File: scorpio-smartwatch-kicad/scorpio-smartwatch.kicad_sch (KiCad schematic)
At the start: 5 parts, among them IC1 LSM6DSV80XTR, U1 nRF52840, U2 MIA-M10Q, U3 LIS2MDL

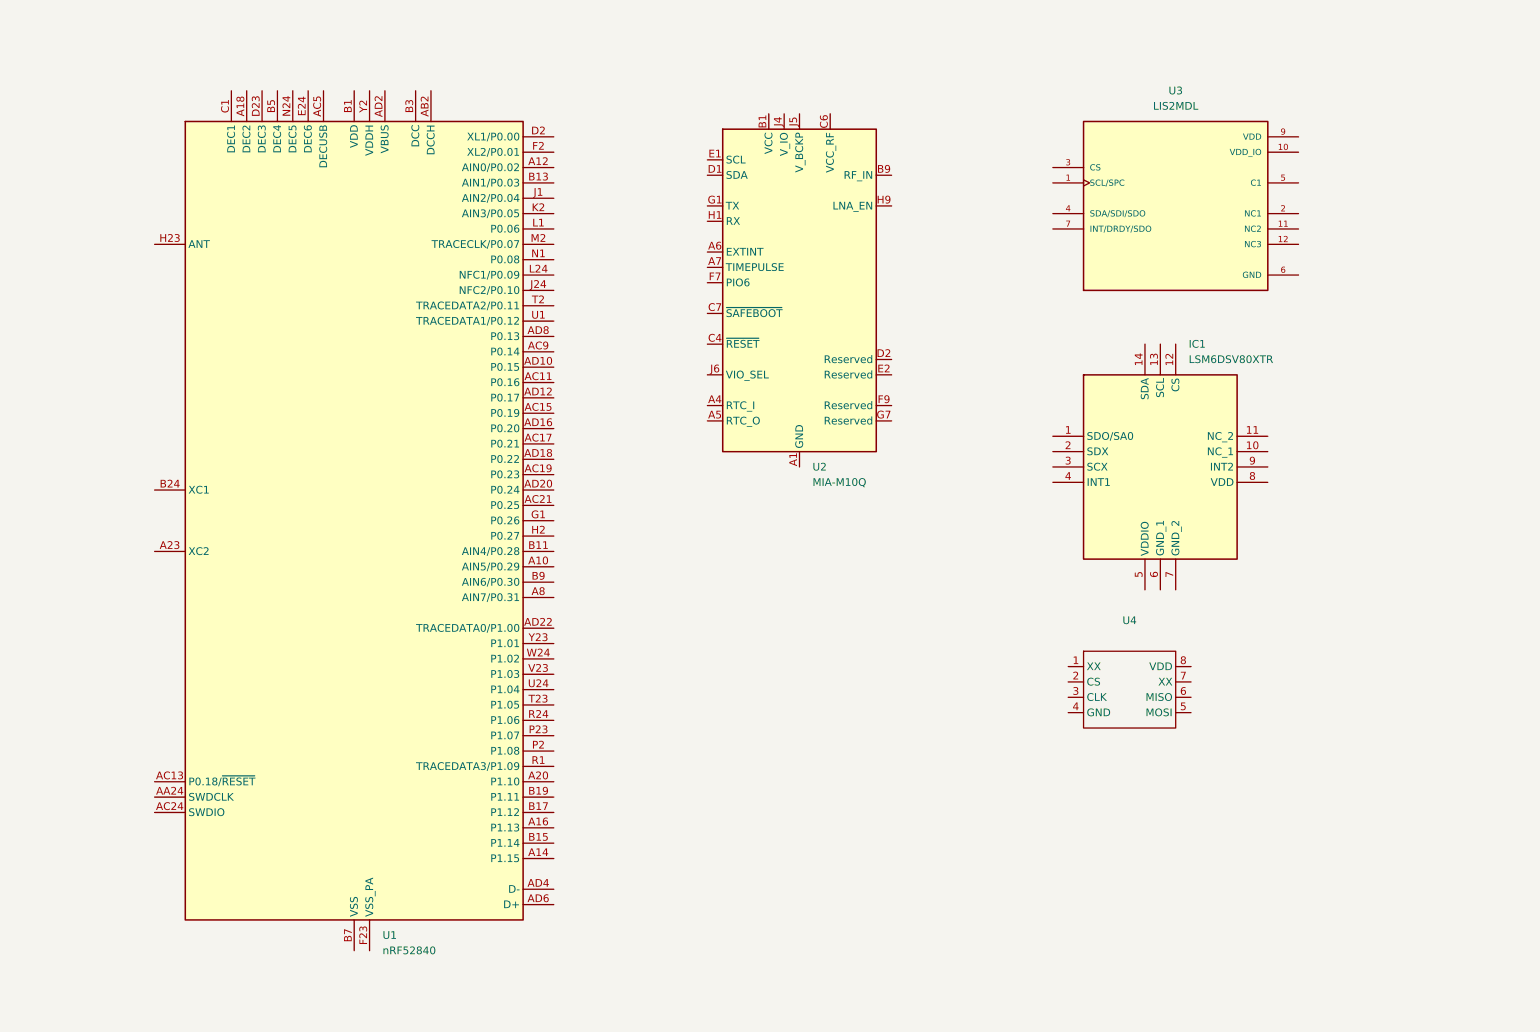
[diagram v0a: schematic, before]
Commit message: Adding dimensions on the pcb and adding tables for current and battery sizes. need to change NRF footprint still. Need to add: Buttons, Screen Connector / Driver, HR connector (I2C), Power Management, Battery Connector, Mounting Holes, Passives.
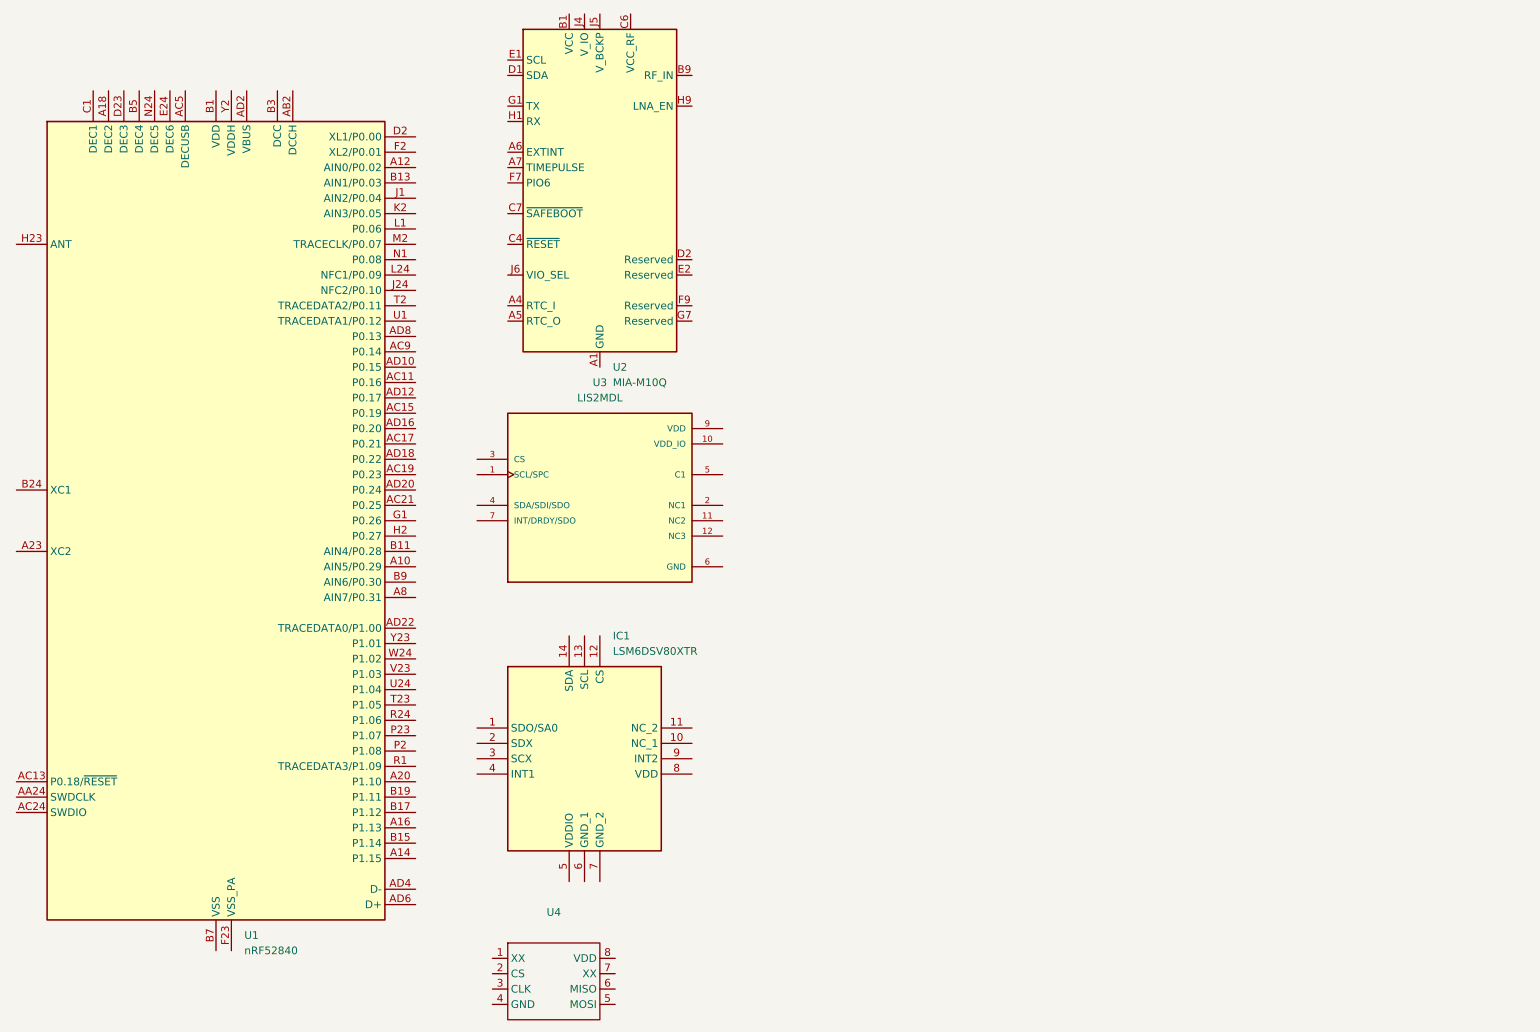
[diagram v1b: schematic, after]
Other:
- moved on the sheet: IC1, U1, U2, U3, U4

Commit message: minor changes
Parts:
- removed U1: nRF52840, Package_DFN_QFN:Nordic_AQFN-73-1EP_7x7mm_P0.5mm, symbol MCU_Nordic:nRF52840
- added IC2: NRF52840-QFAA-F-R, RF_Module:QFN40P600X600X95-49N-D, symbol MCU_Nordic:NRF52840-QFAA-F-R
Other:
- note added: "NEEDS: - Chip antennas - Buttons - Display Connector - HR Sensor Connector (I2C) - Programming Header (JTAG / SWD) - Power LED - Status LED - Power Connection - Battery Charger - Passives"
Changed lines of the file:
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@@
 	(generator_version "9.0")
 	(paper "A4")
+	(text "NEEDS:\n- Chip antennas\n- Buttons\n- Display Connector\n- HR Sensor Connector (I2C)\n- Programming Header (JTAG / SWD)\n- Power LED\n- Status LED\n- Power Connection\n- Battery Charger\n- Passives"
+		(exclude_from_sim no)
+		(at 166.624 101.092 0)
+		(effects
+			(font
+				(size 3 3)
+				(thickness 0.6)
+				(bold yes)
+			)
+			(justify left)
+		)
+	)
 	(table
 		(column_count 3)
@@
 					)
 					(justify left top)
-				)
-			)
-		)
-	)
-	(symbol
-		(lib_id "MCU_Nordic:nRF52840")
-		(at 54.61 104.14 0)
-		(unit 1)
-		(exclude_from_sim no)
-		(in_bom yes)
-		(on_board yes)
-		(dnp no)
-		(fields_autoplaced yes)
-		(property "Reference" "U1"
-			(at 59.2933 172.72 0)
-			(effects
-				(font
-					(size 1.27 1.27)
-				)
-				(justify left)
-			)
-		)
-		(property "Value" "nRF52840"
-			(at 59.2933 175.26 0)
-			(effects
-				(font
-					(size 1.27 1.27)
-				)
-				(justify left)
-			)
-		)
-		(property "Footprint" "Package_DFN_QFN:Nordic_AQFN-73-1EP_7x7mm_P0.5mm"
-			(at 54.61 177.8 0)
-			(effects
-				(font
-					(size 1.27 1.27)
-				)
-				(hide yes)
-			)
-		)
-		(property "Datasheet" "http://infocenter.nordicsemi.com/topic/com.nordic.infocenter.nrf52/dita/nrf52/chips/nrf52840.html"
-			(at 38.1 55.88 0)
-			(effects
-				(font
-					(size 1.27 1.27)
-				)
-				(hide yes)
-			)
-		)
-		(property "Description" "Multiprotocol BLE/ANT/2.4 GHz/802.15.4 Cortex-M4F SoC, AQFN-73"
-			(at 54.61 104.14 0)
-			(effects
-				(font
-					(size 1.27 1.27)
-				)
-				(hide yes)
-			)
-		)
-		(pin "B7"
-		)
-		(pin "E24"
-		)
-		(pin "AD2"
-		)
-		(pin "B3"
-		)
-		(pin "AB2"
-		)
-		(pin "D2"
-		)
-		(pin "F2"
-		)
-		(pin "A12"
-		)
-		(pin "B13"
-		)
-		(pin "J1"
-		)
-		(pin "K2"
-		)
-		(pin "L1"
-		)
-		(pin "M2"
-		)
-		(pin "N1"
-		)
-		(pin "L24"
-		)
-		(pin "J24"
-		)
-		(pin "Y2"
-		)
-		(pin "F23"
-		)
-		(pin "B1"
-		)
-		(pin "AD23"
-		)
-		(pin "AC5"
-		)
-		(pin "AA24"
-		)
-		(pin "AC24"
-		)
-		(pin "T2"
-		)
-		(pin "U1"
-		)
-		(pin "AD8"
-		)
-		(pin "AC9"
-		)
-		(pin "AD10"
-		)
-		(pin "AC11"
-		)
-		(pin "AD12"
-		)
-		(pin "AC15"
-		)
-		(pin "AD16"
-		)
-		(pin "AC17"
-		)
-		(pin "AD18"
-		)
-		(pin "AC19"
-		)
-		(pin "AD20"
-		)
-		(pin "AC21"
-		)
-		(pin "G1"
-		)
-		(pin "H2"
-		)
-		(pin "B11"
-		)
-		(pin "A10"
-		)
-		(pin "B9"
-		)
-		(pin "A8"
-		)
-		(pin "AD22"
-		)
-		(pin "Y23"
-		)
-		(pin "W24"
-		)
-		(pin "V23"
-		)
-		(pin "U24"
-		)
-		(pin "T23"
-		)
-		(pin "R24"
-		)
-		(pin "P23"
-		)
-		(pin "P2"
-		)
-		(pin "R1"
-		)
-		(pin "A20"
-		)
-		(pin "B19"
-		)
-		(pin "B17"
-		)
-		(pin "A16"
-		)
-		(pin "B15"
-		)
-		(pin "A14"
-		)
-		(pin "AD4"
-		)
-		(pin "AD6"
-		)
-		(pin "AC13"
-		)
-		(pin "AD14"
-		)
-		(pin "C1"
-		)
-		(pin "B5"
-		)
-		(pin "A22"
-		)
-		(pin "A23"
-		)
-		(pin "B24"
-		)
-		(pin "H23"
-		)
-		(pin "W1"
-		)
-		(pin "N24"
-		)
-		(pin "A18"
-		)
-		(pin "EP"
-		)
-		(pin "D23"
-		)
-		(instances
-			(project ""
-				(path "/96827652-e1e2-460c-809b-37b17a1aacc0"
-					(reference "U1")
-					(unit 1)
 				)
 			)
@@
 					(unit 1)
 				)
+			)
+		)
+	)
+	(symbol
+		(lib_id "MCU_Nordic:NRF52840-QFAA-F-R")
+		(at 27.94 85.09 0)
+		(unit 1)
+		(exclude_from_sim no)
+		(in_bom yes)
+		(on_board yes)
+		(dnp no)
+		(fields_autoplaced yes)
+		(property "Reference" "IC2"
+			(at 86.36 78.6698 0)
+			(effects
+				(font
+					(size 1.27 1.27)
+				)
+			)
+		)
+		(property "Value" "NRF52840-QFAA-F-R"
+			(at 86.36 81.2098 0)
+			(effects
+				(font
+					(size 1.27 1.27)
+				)
+			)
+		)
+		(property "Footprint" "RF_Module:QFN40P600X600X95-49N-D"
+			(at 74.93 164.77 0)
+			(effects
+				(font
+					(size 1.27 1.27)
+				)
+				(justify left top)
+				(hide yes)
+			)
+		)
+		(property "Datasheet" "https://docs-be.nordicsemi.com/bundle/ps_nrf52840/attach/nRF52840_PS_v1.11.pdf?_LANG=enus"
+			(at 74.93 264.77 0)
+			(effects
+				(font
+					(size 1.27 1.27)
+				)
+				(justify left top)
+				(hide yes)
+			)
+		)
+		(property "Description" "RF System on a Chip - SoC Multiprotocol Bluetooth 5.3 SoC supporting Bluetooth Low Energy, Bluetooth mesh, NFC, Thread and Zigbee"
+			(at 27.94 85.09 0)
+			(effects
+				(font
+					(size 1.27 1.27)
+				)
+				(hide yes)
+			)
+		)
+		(property "Height" "0.95"
+			(at 74.93 464.77 0)
+			(effects
+				(font
+					(size 1.27 1.27)
+				)
+				(justify left top)
+				(hide yes)
+			)
+		)
+		(property "Mouser Part Number" "949-NRF52840QFAA-R"
+			(at 74.93 564.77 0)
+			(effects
+				(font
+					(size 1.27 1.27)
+				)
+				(justify left top)
+				(hide yes)
+			)
+		)
+		(property "Mouser Price/Stock" "https://www.mouser.co.uk/ProductDetail/Nordic-Semiconductor/NRF52840-QFAA-F-R?qs=A6eO%252BMLsxmSdeoxcrQ6IBg%3D%3D"
+			(at 74.93 664.77 0)
+			(effects
+				(font
+					(size 1.27 1.27)
+				)
+				(justify left top)
+				(hide yes)
+			)
+		)
+		(property "Manufacturer_Name" "Nordic Semiconductor"
+			(at 74.93 764.77 0)
+			(effects
+				(font
+					(size 1.27 1.27)
+				)
+				(justify left top)
+				(hide yes)
+			)
+		)
+		(property "Manufacturer_Part_Number" "NRF52840-QFAA-F-R"
+			(at 74.93 864.77 0)
+			(effects
+				(font
+					(size 1.27 1.27)
+				)
+				(justify left top)
+				(hide yes)
+			)
+		)
+		(pin "46"
+		)
+		(pin "28"
+		)
+		(pin "27"
+		)
+		(pin "26"
+		)
+		(pin "25"
+		)
+		(pin "34"
+		)
+		(pin "33"
+		)
+		(pin "32"
+		)
+		(pin "31"
+		)
+		(pin "30"
+		)
+		(pin "29"
+		)
+		(pin "37"
+		)
+		(pin "36"
+		)
+		(pin "35"
+		)
+		(pin "23"
+		)
+		(pin "38"
+		)
+		(pin "24"
+		)
+		(pin "10"
+		)
+		(pin "49"
+		)
+		(pin "17"
+		)
+		(pin "44"
+		)
+		(pin "9"
+		)
+		(pin "8"
+		)
+		(pin "7"
+		)
+		(pin "6"
+		)
+		(pin "20"
+		)
+		(pin "2"
+		)
+		(pin "3"
+		)
+		(pin "11"
+		)
+		(pin "14"
+		)
+		(pin "5"
+		)
+		(pin "4"
+		)
+		(pin "45"
+		)
+		(pin "48"
+		)
+		(pin "12"
+		)
+		(pin "15"
+		)
+		(pin "16"
+		)
+		(pin "1"
+		)
+		(pin "41"
+		)
+		(pin "21"
+		)
+		(pin "40"
+		)
+		(pin "19"
+		)
+		(pin "22"
+		)
+		(pin "43"
+		)
+		(pin "39"
+		)
+		(pin "42"
+		)
+		(pin "47"
+		)
+		(pin "18"
+		)
+		(pin "13"
+		)
+		(instances
+			(project ""
+				(path "/96827652-e1e2-460c-809b-37b17a1aacc0"
+					(reference "IC2")
+					(unit 1)
+				)

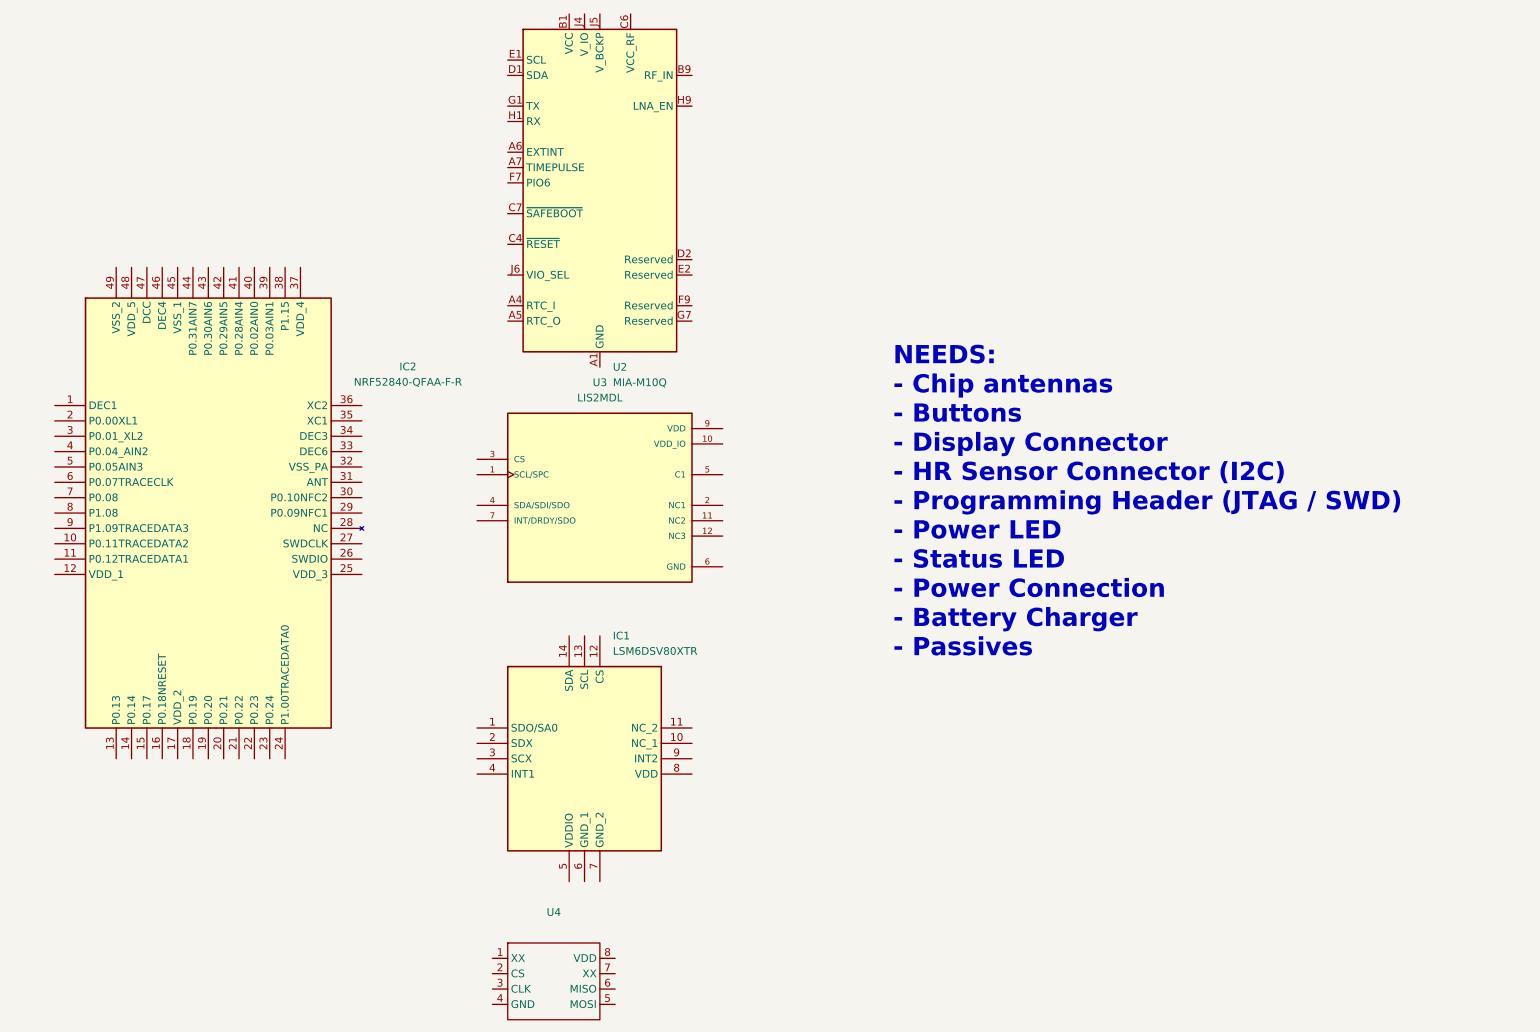
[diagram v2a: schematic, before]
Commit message: wip commit, added chip antenna, trying out different pcb sizes. not routing until we can figure out the rf nightmare with ground plane sizes.
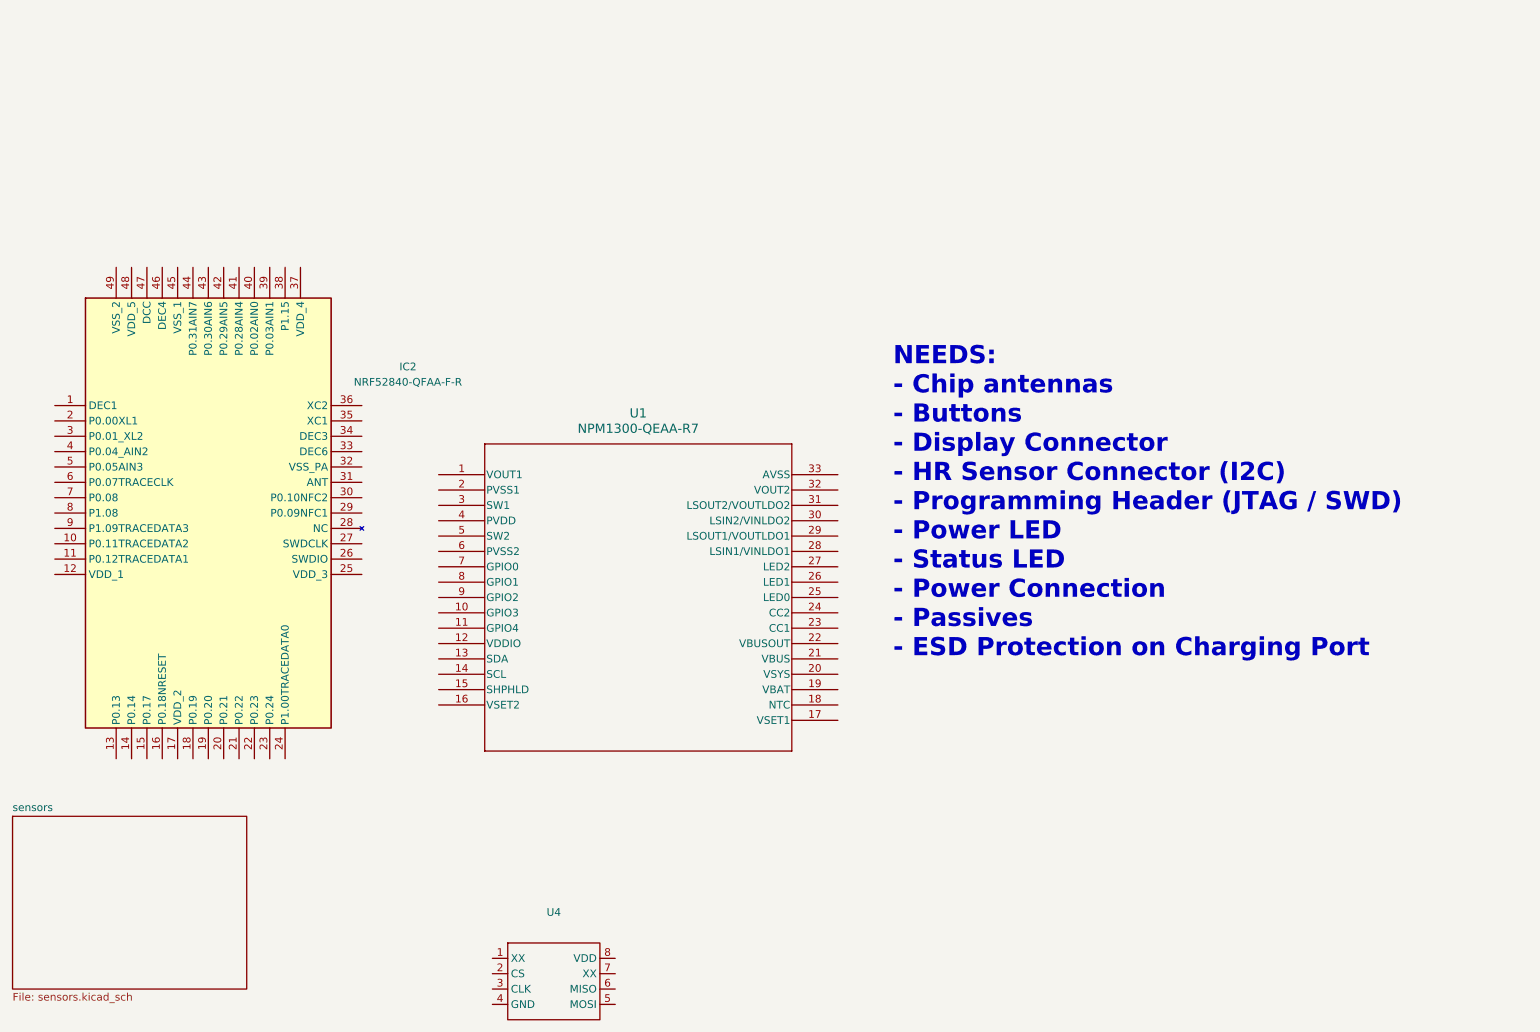
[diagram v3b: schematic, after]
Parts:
- removed IC1: LSM6DSV80XTR, LSM6DSV16BXTR, symbol LSM6DSV80XTR:LSM6DSV80XTR
- removed U2: MIA-M10Q, Package_LGA:ublox_LGA-53_4.5x4.5mm_Layout9x9_P0.5mm, symbol RF_GPS:MIA-M10Q
- removed U3: LIS2MDL, LIS2MDL:PQFN50P200X200X70-12N, symbol LIS2MDL:LIS2MDL
- added U1: NPM1300-QEAA-R7, NPM1300:QFN32_5X5_NOR-M, symbol NPM1300:NPM1300-QEAA-R7
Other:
- added sheet sensors (sensors.kicad_sch)
- note added: "NEEDS: - Chip antennas - Buttons - Display Connector - HR Sensor Connector (I2C) - Programming Header (JTAG / SWD) - Power LED - Status LED - Power Connection - Passives - ESD Protection on Charging Port"
- note removed: "NEEDS: - Chip antennas - Buttons - Display Connector - HR Sensor Connector (I2C) - Programming Header (JTAG / SWD) - Power LED - Status LED - Power Connection - Battery Charger - Passives"
